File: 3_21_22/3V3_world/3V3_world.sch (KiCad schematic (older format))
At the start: 10 parts

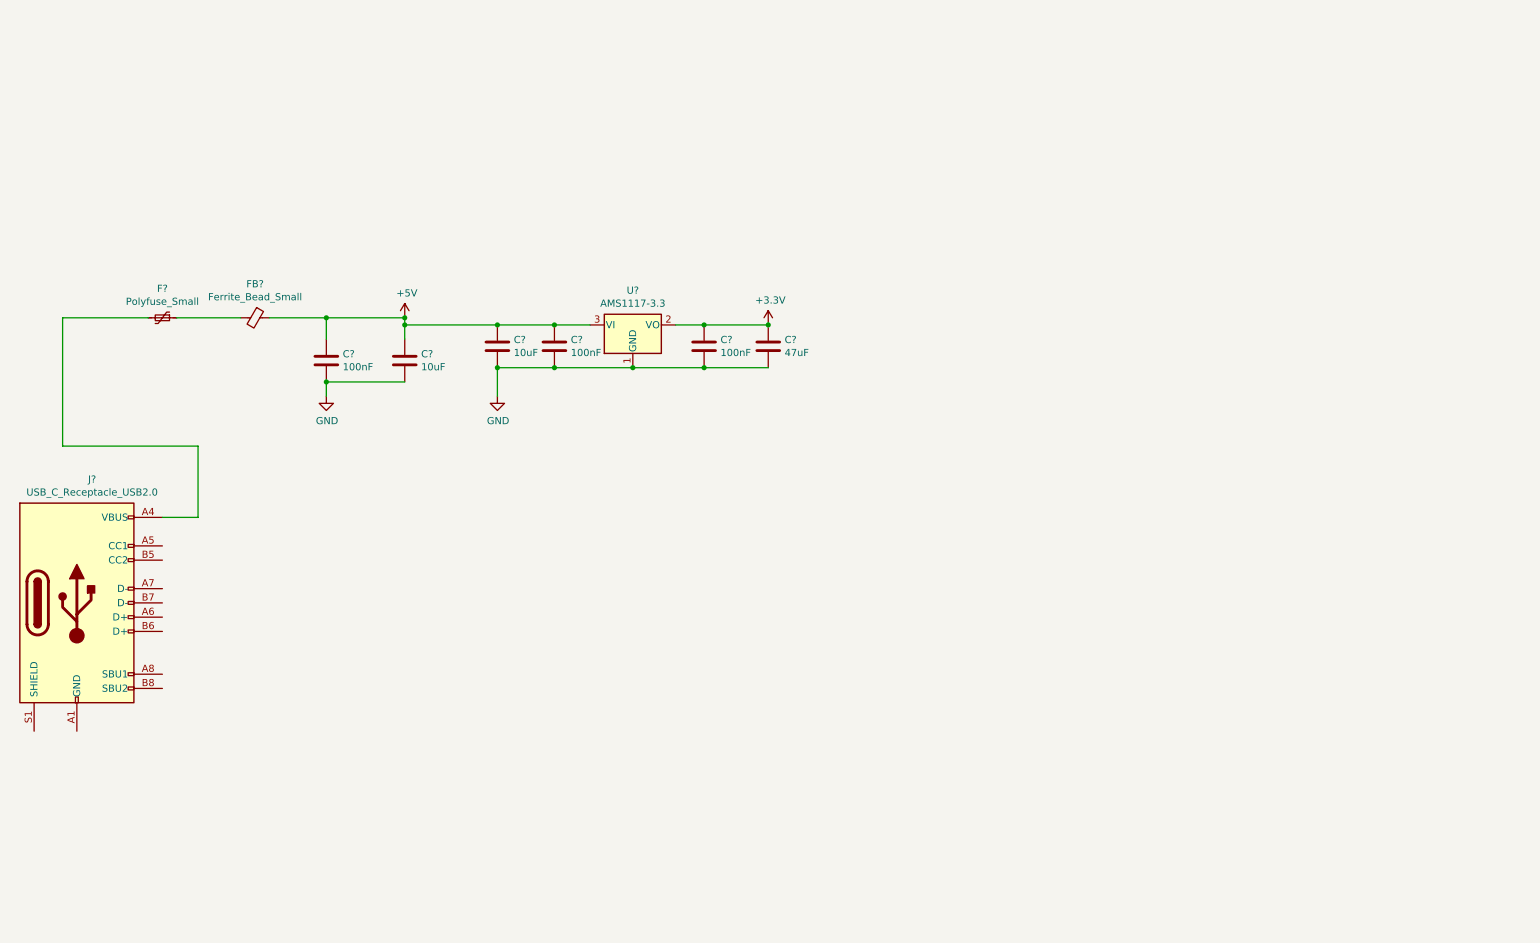
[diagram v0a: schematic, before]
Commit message: Added 5to12Buck
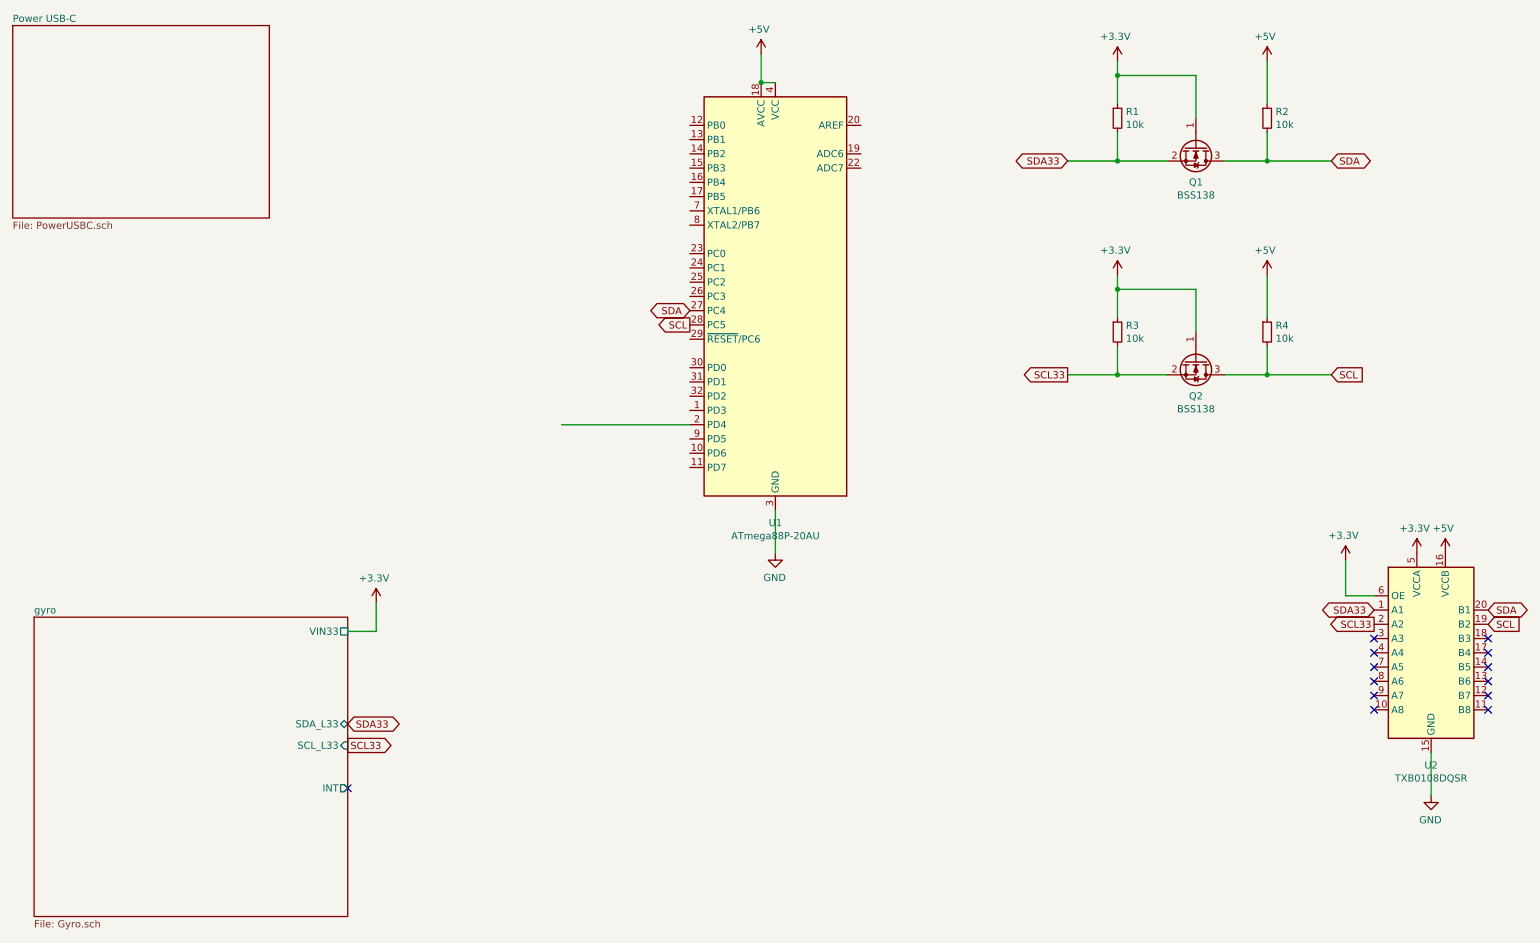
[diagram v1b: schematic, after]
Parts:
- removed C? (x3): 100nF, symbol Device:C
- removed C? (x2): 10uF, symbol Device:C
- removed C?: 47uF, symbol Device:C
- removed F?: Polyfuse_Small, symbol Device:Polyfuse_Small
- removed FB?: Ferrite_Bead_Small, symbol Device:Ferrite_Bead_Small
- removed J?: USB_C_Receptacle_USB2.0, symbol Connector:USB_C_Receptacle_USB2.0
- removed U?: AMS1117-3.3, Package_TO_SOT_SMD:SOT-223-3_TabPin2, symbol Regulator_Linear:AMS1117-3.3
- added Q1, Q2: BSS138, Package_TO_SOT_SMD:SOT-23, symbol Transistor_FET:BSS138
- added R1, R2, R3, R4: 10k, symbol Device:R_Small
- added U1: ATmega88P-20AU, Package_QFP:TQFP-32_7x7mm_P0.8mm, symbol MCU_Microchip_ATmega:ATmega88P-20AU
- added U2: TXB0108DQSR, Package_SON:USON-20_2x4mm_P0.4mm, symbol Logic_LevelTranslator:TXB0108DQSR
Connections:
- net labels added: SCL, SCL33, SDA, SDA33
- wire segments 23 -> 31
- no-connect marks 0 -> 13
